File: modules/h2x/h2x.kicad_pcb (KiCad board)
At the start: 2 copper layers, 40.6 x 40.6 mm, 44 parts, among them J1 2, J10 11, J11 12, J12 13, J13 A0, J14 A1, J15 A2, J16 A3, J17 A4, J18 A5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

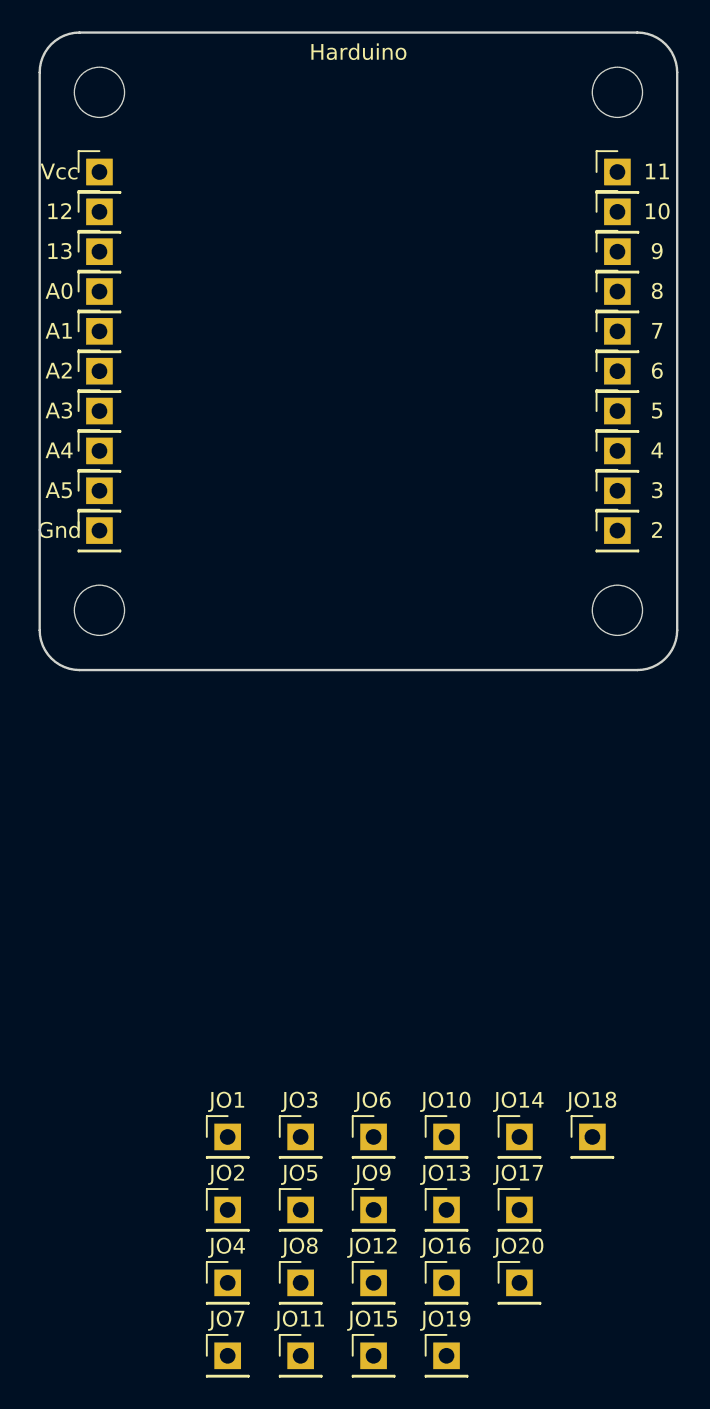
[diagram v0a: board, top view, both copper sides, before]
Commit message: Place connectors
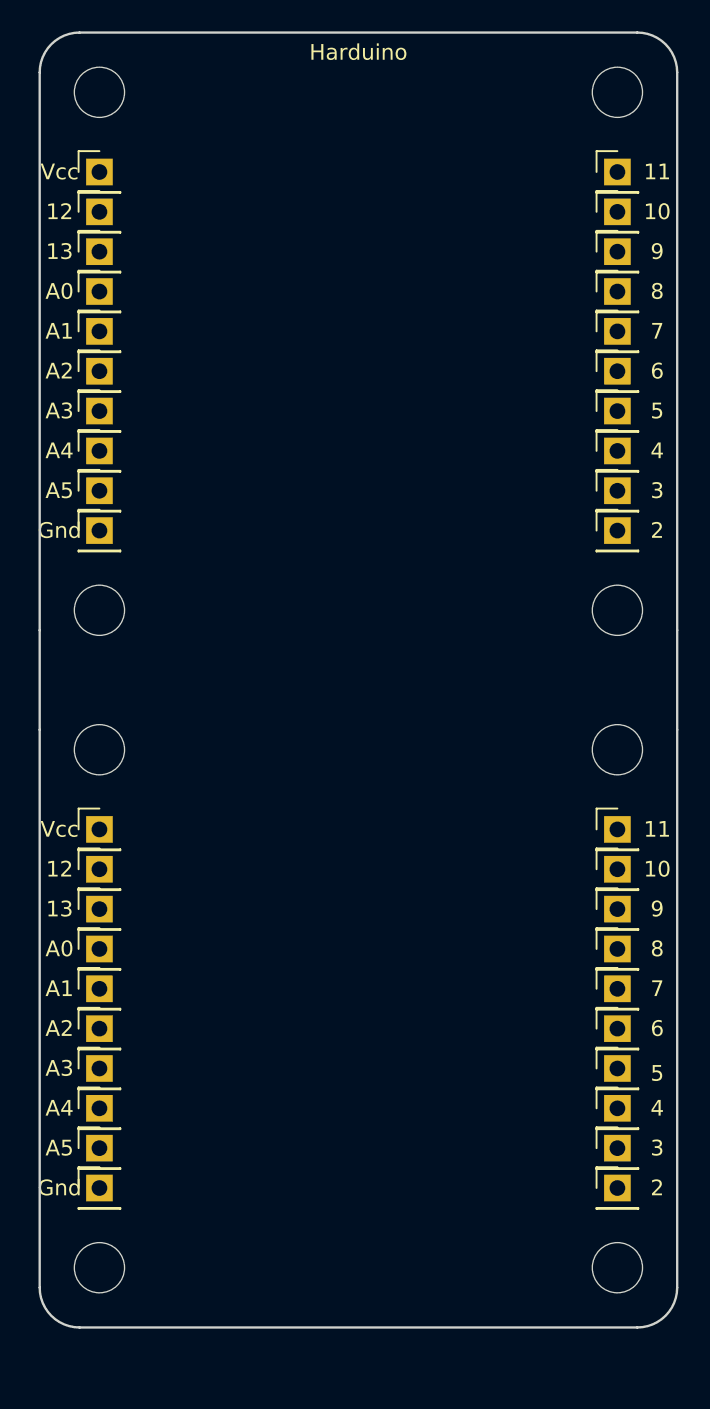
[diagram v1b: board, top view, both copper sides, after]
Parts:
- added H1: MountingHole, MountingHole:MountingHole_3.2mm_M3, F.Cu at (92.7, 96.5)
- added H2: MountingHole, MountingHole:MountingHole_3.2mm_M3, F.Cu at (92.7, 129.5)
- added H3: MountingHole, MountingHole:MountingHole_3.2mm_M3, F.Cu at (125.7, 96.5)
- added H4: MountingHole, MountingHole:MountingHole_3.2mm_M3, F.Cu at (125.7, 129.5)
- moved JO19 40.2 mm to (92.7, 101.6)
- moved JO7 35.9 mm to (125.7, 109.2)
- moved JO11 33.6 mm to (92.7, 104.1)
- moved JO18 31.4 mm to (92.7, 121.9)
- moved JO8 31.2 mm to (125.7, 106.7)
- moved JO12 29.5 mm to (92.7, 106.7)
- moved JO14 28.4 mm to (92.7, 111.8)
- moved JO4 28.4 mm to (125.7, 116.8)
- moved JO13 27.7 mm to (92.7, 109.2)
- moved JO17 27.5 mm to (92.7, 119.4)
- moved JO20 27.4 mm to (92.7, 124.5)
- moved JO15 27.2 mm to (92.7, 114.3)
- moved JO9 26.7 mm to (125.7, 104.1)
- moved JO16 26.0 mm to (92.7, 116.8)
- moved JO2 25.2 mm to (125.7, 121.9)
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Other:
- board size 40.6 x 40.6 mm -> 40.6 x 82.5 mm

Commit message: Try to add some traces to 2x board
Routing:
- net Net-(J19-Pad1): track 0.00 -> 78.1 mm, vias 0 -> 2
- net Net-(J11-Pad1): track 0.00 -> 74.9 mm, vias 0 -> 2
- net Net-(J12-Pad1): track 0.00 -> 71.8 mm, vias 0 -> 2
- net Net-(J13-Pad1): track 0.00 -> 68.6 mm, vias 0 -> 2
- net Net-(J14-Pad1): track 0.00 -> 65.4 mm, vias 0 -> 2
- net Net-(J15-Pad1): track 0.00 -> 62.2 mm, vias 0 -> 2
- net Net-(J16-Pad1): track 0.00 -> 59.1 mm, vias 0 -> 2
- net Net-(J17-Pad1): track 0.00 -> 55.9 mm, vias 0 -> 2
- net Net-(J18-Pad1): track 0.00 -> 52.7 mm, vias 0 -> 2
- net Net-(J20-Pad1): track 0.00 -> 49.5 mm, vias 0 -> 2
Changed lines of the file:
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@@
     (thickness 1.6)
     (drawings 53)
-    (tracks 0)
+    (tracks 53)
     (zones 0)
     (modules 48)
@@
   )
   (setup
-    (last_trace_width 0.25)
+    (last_trace_width 0.8)
+    (user_trace_width 0.6)
+    (user_trace_width 0.8)
     (trace_clearance 0.2)
     (zone_clearance 0.508)
@@
     (via_min_size 0.4)
     (via_min_drill 0.3)
+    (user_via 1.5 0.9)
     (uvia_size 0.3)
     (uvia_drill 0.1)
@@
   (gr_line (start 129.54 53.34) (end 129.54 88.9) (layer Edge.Cuts) (width 0.15))
   (gr_line (start 91.44 50.8) (end 127 50.8) (layer Edge.Cuts) (width 0.15))
+  (via (at 109.22 62.23) (size 1.5) (drill 0.9) (layers F.Cu B.Cu) (net 11))
+  (segment (start 109.22 62.23) (end 109.22 104.14) (width 0.8) (layer F.Cu) (net 11))
+  (via (at 109.22 104.14) (size 1.5) (drill 0.9) (layers F.Cu B.Cu) (net 11))
+  (segment (start 92.71 62.23) (end 109.22 62.23) (width 0.8) (layer B.Cu) (net 11))
+  (segment (start 92.71 104.14) (end 109.22 104.14) (width 0.8) (layer B.Cu) (net 11))
+  (via (at 107.6325 64.77) (size 1.5) (drill 0.9) (layers F.Cu B.Cu) (net 12))
+  (segment (start 107.6325 64.77) (end 107.6325 106.68) (width 0.8) (layer F.Cu) (net 12))
+  (via (at 107.6325 106.68) (size 1.5) (drill 0.9) (layers F.Cu B.Cu) (net 12))
+  (segment (start 94.36 64.77) (end 107.6325 64.77) (width 0.8) (layer B.Cu) (net 12))
+  (segment (start 92.71 64.77) (end 94.36 64.77) (width 0.8) (layer B.Cu) (net 12))
+  (segment (start 92.71 106.68) (end 107.6325 106.68) (width 0.8) (layer B.Cu) (net 12))
+  (via (at 106.045 67.31) (size 1.5) (drill 0.9) (layers F.Cu B.Cu) (net 13))
+  (segment (start 106.045 67.31) (end 106.045 109.22) (width 0.8) (layer F.Cu) (net 13))
+  (via (at 106.045 109.22) (size 1.5) (drill 0.9) (layers F.Cu B.Cu) (net 13))
+  (segment (start 92.71 67.31) (end 106.045 67.31) (width 0.8) (layer B.Cu) (net 13))
+  (segment (start 92.71 109.22) (end 106.045 109.22) (width 0.8) (layer B.Cu) (net 13))
+  (via (at 104.4575 69.85) (size 1.5) (drill 0.9) (layers F.Cu B.Cu) (net 14))
+  (segment (start 104.4575 69.85) (end 104.4575 111.76) (width 0.8) (layer F.Cu) (net 14))
+  (via (at 104.4575 111.76) (size 1.5) (drill 0.9) (layers F.Cu B.Cu) (net 14))
+  (segment (start 92.71 69.85) (end 104.4575 69.85) (width 0.8) (layer B.Cu) (net 14))
+  (segment (start 92.71 111.76) (end 104.4575 111.76) (width 0.8) (layer B.Cu) (net 14))
+  (via (at 102.87 72.39) (size 1.5) (drill 0.9) (layers F.Cu B.Cu) (net 15))
+  (segment (start 102.87 72.39) (end 102.87 114.3) (width 0.8) (layer F.Cu) (net 15))
+  (via (at 102.87 114.3) (size 1.5) (drill 0.9) (layers F.Cu B.Cu) (net 15))
+  (segment (start 92.71 72.39) (end 102.87 72.39) (width 0.8) (layer B.Cu) (net 15))
+  (segment (start 92.71 114.3) (end 102.87 114.3) (width 0.8) (layer B.Cu) (net 15))
+  (via (at 101.2825 74.93) (size 1.5) (drill 0.9) (layers F.Cu B.Cu) (net 16))
+  (segment (start 101.2825 74.93) (end 101.2825 116.84) (width 0.8) (layer F.Cu) (net 16))
+  (via (at 101.2825 116.84) (size 1.5) (drill 0.9) (layers F.Cu B.Cu) (net 16))
+  (segment (start 92.71 74.93) (end 101.2825 74.93) (width 0.8) (layer B.Cu) (net 16))
+  (segment (start 92.71 116.84) (end 101.2825 116.84) (width 0.8) (layer B.Cu) (net 16))
+  (via (at 99.695 77.47) (size 1.5) (drill 0.9) (layers F.Cu B.Cu) (net 17))
+  (segment (start 99.695 77.47) (end 99.695 119.38) (width 0.8) (layer F.Cu) (net 17))
+  (via (at 99.695 119.38) (size 1.5) (drill 0.9) (layers F.Cu B.Cu) (net 17))
+  (segment (start 92.71 77.47) (end 99.695 77.47) (width 0.8) (layer B.Cu) (net 17))
+  (segment (start 92.71 119.38) (end 99.695 119.38) (width 0.8) (layer B.Cu) (net 17))
+  (via (at 98.1075 80.01) (size 1.5) (drill 0.9) (layers F.Cu B.Cu) (net 18))
+  (via (at 98.1075 121.92) (size 1.5) (drill 0.9) (layers F.Cu B.Cu) (net 18))
+  (segment (start 98.1075 80.01) (end 98.1075 121.92) (width 0.8) (layer F.Cu) (net 18))
+  (segment (start 92.71 80.01) (end 98.1075 80.01) (width 0.8) (layer B.Cu) (net 18))
+  (segment (start 92.71 121.92) (end 98.1075 121.92) (width 0.8) (layer B.Cu) (net 18))
+  (via (at 110.8075 59.69) (size 1.5) (drill 0.9) (layers F.Cu B.Cu) (net 19))
+  (segment (start 110.8075 59.69) (end 110.8075 101.6) (width 0.8) (layer F.Cu) (net 19))
+  (via (at 110.8075 101.6) (size 1.5) (drill 0.9) (layers F.Cu B.Cu) (net 19))
+  (segment (start 92.71 59.69) (end 110.8075 59.69) (width 0.8) (layer B.Cu) (net 19))
+  (segment (start 92.71 101.6) (end 110.8075 101.6) (width 0.8) (layer B.Cu) (net 19))
+  (segment (start 92.71 82.55) (end 96.52 82.55) (width 0.8) (layer B.Cu) (net 20))
+  (segment (start 96.52 124.46) (end 96.52 82.55) (width 0.8) (layer F.Cu) (net 20))
+  (segment (start 96.52 124.46) (end 96.52 124.46) (width 0.8) (layer B.Cu) (net 20))
+  (segment (start 96.52 82.55) (end 96.52 82.55) (width 0.8) (layer B.Cu) (net 20))
+  (via (at 96.52 82.55) (size 1.5) (drill 0.9) (layers F.Cu B.Cu) (net 20))
+  (segment (start 96.52 124.46) (end 92.71 124.46) (width 0.8) (layer B.Cu) (net 20))
+  (via (at 96.52 124.46) (size 1.5) (drill 0.9) (layers F.Cu B.Cu) (net 20) (status 1000000))
 )

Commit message: h2x ready
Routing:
- net Net-(J1-Pad1): track 0.00 -> 72.4 mm, vias 0 -> 2
- net Net-(J2-Pad1): track 0.00 -> 69.9 mm, vias 0 -> 2
- net Net-(J3-Pad1): track 0.00 -> 67.3 mm, vias 0 -> 2
- net Net-(J4-Pad1): track 0.00 -> 64.8 mm, vias 0 -> 2
- net Net-(J5-Pad1): track 0.00 -> 62.2 mm, vias 0 -> 2
- net Net-(J6-Pad1): track 0.00 -> 59.7 mm, vias 0 -> 2
- net Net-(J7-Pad1): track 0.00 -> 57.2 mm, vias 0 -> 2
- net Net-(J8-Pad1): track 0.00 -> 54.6 mm, vias 0 -> 2
- net Net-(J9-Pad1): track 0.00 -> 52.1 mm, vias 0 -> 2
- net Net-(J10-Pad1): track 0.00 -> 49.5 mm, vias 0 -> 2
- net Net-(J19-Pad1): track 78.1 -> 72.4 mm
- net Net-(J11-Pad1): track 74.9 -> 69.9 mm
- net Net-(J12-Pad1): track 71.8 -> 67.3 mm
- net Net-(J13-Pad1): track 68.6 -> 64.8 mm
- net Net-(J14-Pad1): track 65.4 -> 62.2 mm
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
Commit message: Harduino -> HardDuino
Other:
- board text added: "HardDuino"
- board text removed: "Harduino"
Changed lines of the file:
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@@
   )
   (setup
-    (last_trace_width 0.8)
+    (last_trace_width 0.25)
     (user_trace_width 0.6)
     (user_trace_width 0.8)
@@
   (gr_line (start 129.54 95.25) (end 129.54 130.81) (layer Edge.Cuts) (width 0.15))
   (gr_line (start 88.9 130.81) (end 88.9 95.25) (layer Edge.Cuts) (width 0.15))
-  (gr_text Harduino (at 109.22 52.07) (layer F.SilkS)
-    (effects (font (size 1 1) (thickness 0.15)))
-  )
+  (gr_text HardDuino (at 109.22 52.07) (layer F.SilkS)
+    (effects (font (size 1 1) (thickness 0.15)))
+  )
